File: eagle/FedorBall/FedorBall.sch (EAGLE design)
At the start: 4 parts, among them IC1 MEGA16-P

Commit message: eagle scheme scratch
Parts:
- removed SV1, SV2: (no value), con-lstb:MA05-2
- added C4: (no value), rcl:C-EU050-024X044
- added C5: 100n, rcl:C-EU050-024X044
- added C6: 0.33u, rcl:C-EU050-024X044
- added C7: 0.1u, rcl:C-EU050-024X044
- added C8: 47u, rcl:C-EU050-024X044
- added IC2: 7805T, linear:7805T
- added JP1, JP2: M05X2SHD, SparkFun:M05X2SHD
- added R1, R2, R3, R4: 10k, rcl:R-EU_0207/10
- added X1, X2: 22-23-2041, con-molex:22-23-2041
- S1: device SparkFun:TAC_SWITCHPTH -> SparkFun:TAC_SWITCHKSA_SEALED
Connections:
- new net +5V: C7.1, C8.1, IC1.AVCC, IC1.VCC, IC2.VO, JP1.2, R1.2
- new net GND: C4.2, C5.2, C6.2, C7.2, C8.2, IC1.GND, IC1.GND@1, IC2.GND, JP1.10, JP1.8, S1.1
- new net N$10: IC1.(ADC6)PA6
- new net N$11: IC1.(ADC5)PA5
- new net N$12: IC1.(ADC4)PA4
- new net N$13: IC1.(ADC3)PA3
- new net N$14: IC1.(ADC2)PA2
- new net N$15: IC1.(ADC1)PA1
- new net N$16: IC1.(ADC0)PA0
- new net N$2: C5.1, IC1.AREF
- new net N$5: IC1.(MOSI)PB5, JP1.1, R4.2
- new net N$6: C4.1, IC1.RESET, JP1.5, R1.1, S1.3
- new net N$7: IC1.(SCK)PB7, JP1.7, R2.2
- new net N$8: IC1.(MISO)PB6, JP1.9, R3.2
- new net N$9: IC1.(ADC7)PA7
- new net VCC: C6.1, IC2.VI
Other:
- moved on the sheet: IC1, S1

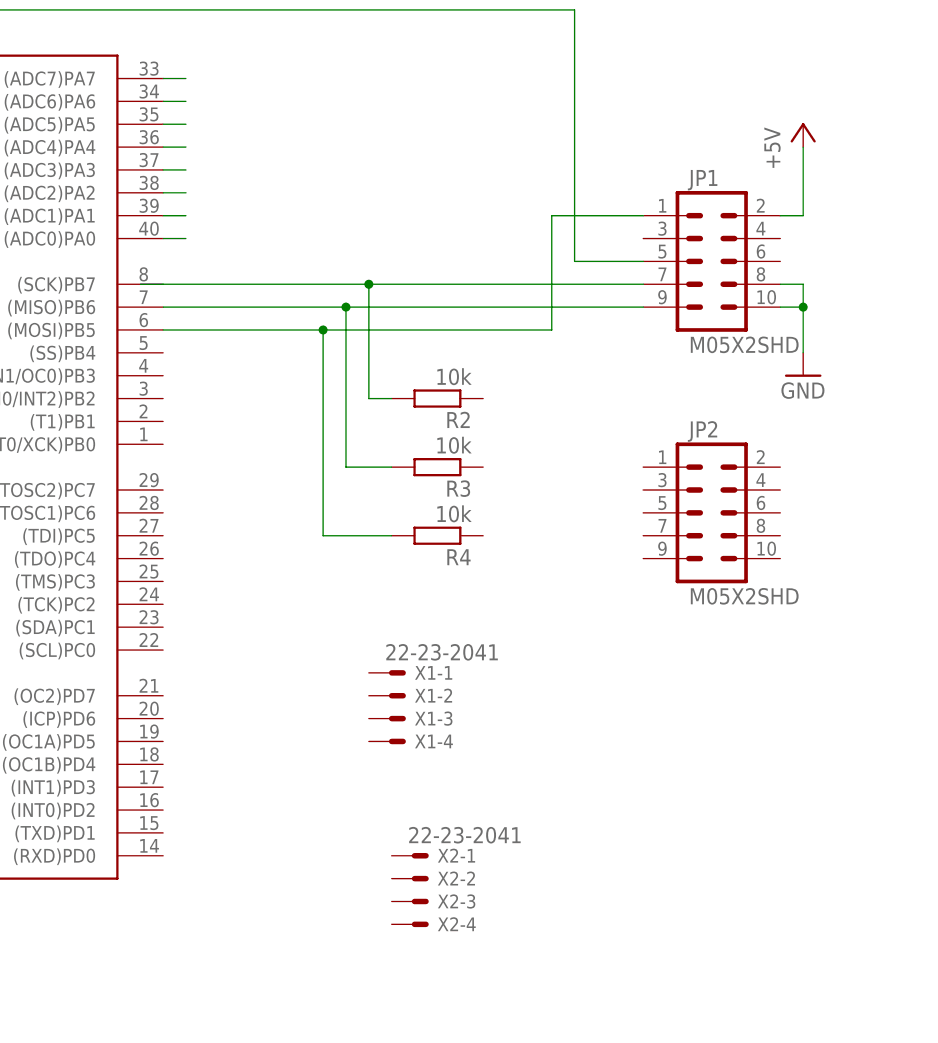
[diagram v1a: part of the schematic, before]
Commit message: update main scheme and board
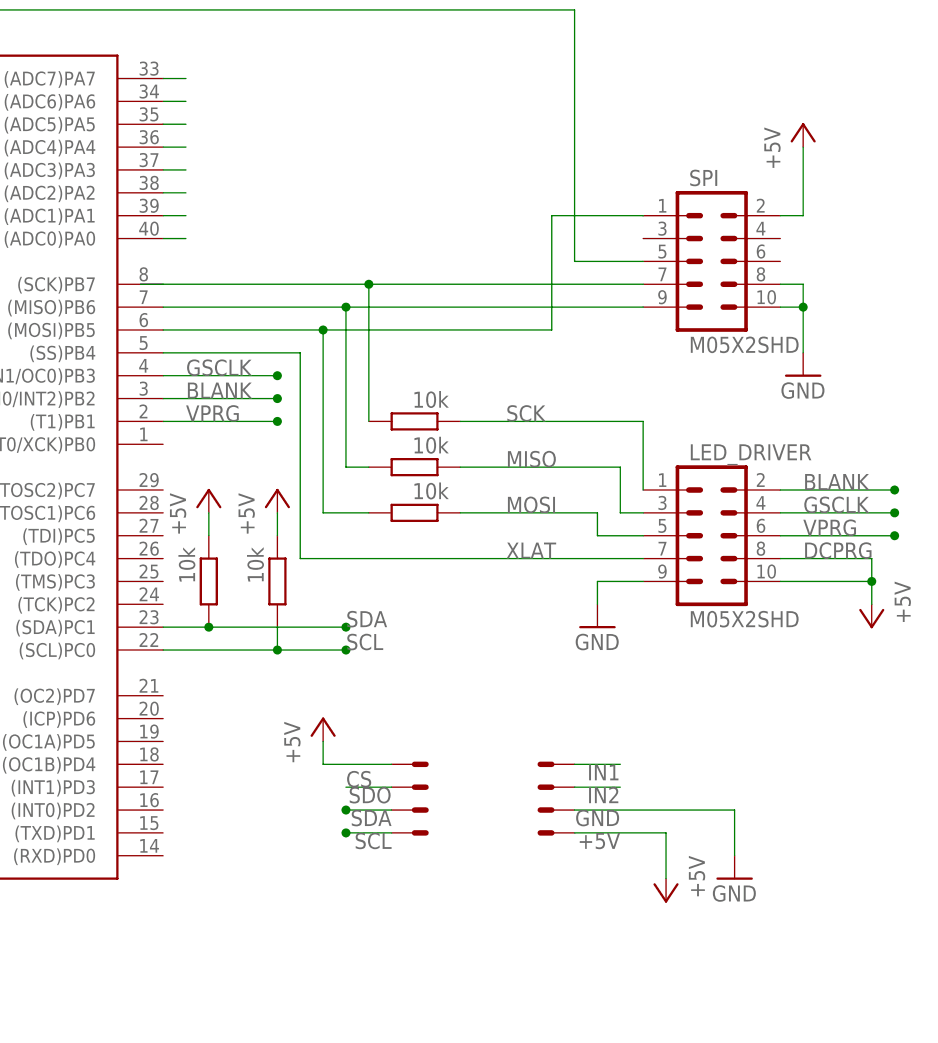
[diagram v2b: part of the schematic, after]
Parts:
- removed JP2: M05X2SHD, SparkFun:M05X2SHD
- added LED_DRIVER: M05X2SHD, SparkFun:M05X2SHD
- added R5, R6: 10k, rcl:R-EU_0207/10
- renumbered JP1 to SPI
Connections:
- new net BLANK: IC1.(AIN0/INT2)PB2, LED_DRIVER.2
- new net GSCLK: IC1.(AIN1/OC0)PB3, LED_DRIVER.4
- new net IN1: X1-4.S
- new net IN2: X1-3.S
- new net MISO: LED_DRIVER.3, R3.1
- new net MOSI: LED_DRIVER.5, R4.1
- new net SCK: LED_DRIVER.1, R2.1
- new net SCL: IC1.(SCL)PC0, R6.2, X2-1.S
- new net SDA: IC1.(SDA)PC1, R5.2, X2-2.S
- new net SDO: X2-3.S
- new net VPRG: IC1.(T1)PB1, LED_DRIVER.6
- new net XLAT: IC1.(SS)PB4, LED_DRIVER.7
- net +5V: now also LED_DRIVER.10, LED_DRIVER.8, R5.1, R6.1, X1-1.S, X2-4.S
- net GND: now also LED_DRIVER.9, X1-2.S
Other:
- note added: "CS"
- note added: "DCPRG"

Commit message: schematic tweaks
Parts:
- C4: value (none) -> 10u
- C5: value 100n -> 0.1u
- R1: value 10k -> 100k
- renumbered SPI to ISP
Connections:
- removed net IN1: X1-4.S
- removed net IN2: X1-3.S
- new net INT0: IC1.(INT1)PD3, X1-4.S
- new net INT1: IC1.(INT0)PD2, X1-3.S
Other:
- note added: "MISO"
- note added: "MOSI"
- note added: "RESET"
- note added: "SCK"
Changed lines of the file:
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@@
 <parts>
 <part name="IC1" library="atmel" deviceset="MEGA16-P" device=""/>
-<part name="C4" library="rcl" deviceset="C-EU" device="050-024X044"/>
-<part name="C5" library="rcl" deviceset="C-EU" device="050-024X044" value="100n"/>
-<part name="R1" library="rcl" deviceset="R-EU_" device="0207/10" value="10k"/>
+<part name="C4" library="rcl" deviceset="C-EU" device="050-024X044" value="10u"/>
+<part name="C5" library="rcl" deviceset="C-EU" device="050-024X044" value="0.1u"/>
+<part name="R1" library="rcl" deviceset="R-EU_" device="0207/10" value="100k"/>
 <part name="GND1" library="supply1" deviceset="GND" device=""/>
 <part name="GND3" library="supply1" deviceset="GND" device=""/>
@@
 <part name="R3" library="rcl" deviceset="R-EU_" device="0207/10" value="10k"/>
 <part name="R4" library="rcl" deviceset="R-EU_" device="0207/10" value="10k"/>
-<part name="SPI" library="SparkFun" deviceset="M05X2" device="SHD"/>
+<part name="ISP" library="SparkFun" deviceset="M05X2" device="SHD"/>
 <part name="LED_DRIVER" library="SparkFun" deviceset="M05X2" device="SHD"/>
 <part name="P+3" library="supply1" deviceset="+5V" device=""/>
@@
 <text x="86.36" y="-15.24" size="1.778" layer="95">DCPRG</text>
 <text x="35.56" y="-40.64" size="1.778" layer="95">CS</text>
+<text x="63.5" y="15.24" size="1.778" layer="95">SCK</text>
+<text x="63.5" y="12.7" size="1.778" layer="95">MISO</text>
+<text x="63.5" y="22.86" size="1.778" layer="95">MOSI</text>
+<text x="60.96" y="17.78" size="1.778" layer="95">RESET</text>
 </plain>
 <instances>
@@
 <instance part="X2" gate="-4" x="43.18" y="-38.1" smashed="yes" rot="MR180"/>
 <instance part="GND4" gate="1" x="-35.56" y="-12.7"/>
-<instance part="SUPPLY1" gate="G$1" x="-76.2" y="-38.1"/>
+<instance part="SUPPLY1" gate="G$1" x="-76.2" y="-30.48"/>
 <instance part="GND6" gate="1" x="-58.42" y="-63.5"/>
 <instance part="C6" gate="G$1" x="-71.12" y="-48.26"/>
@@
 <attribute name="VALUE" x="46.99" y="-6.858" size="1.778" layer="96" rot="R180"/>
 </instance>
-<instance part="SPI" gate="G$1" x="76.2" y="17.78"/>
+<instance part="ISP" gate="G$1" x="76.2" y="17.78"/>
 <instance part="LED_DRIVER" gate="G$1" x="76.2" y="-12.7"/>
 <instance part="P+3" gate="1" x="-35.56" y="-33.02"/>
@@
 <wire x1="83.82" y1="22.86" x2="86.36" y2="22.86" width="0.1524" layer="91"/>
 <wire x1="86.36" y1="22.86" x2="86.36" y2="30.48" width="0.1524" layer="91"/>
-<pinref part="SPI" gate="G$1" pin="2"/>
+<pinref part="ISP" gate="G$1" pin="2"/>
 </segment>
 <segment>
@@
 <wire x1="83.82" y1="12.7" x2="86.36" y2="12.7" width="0.1524" layer="91"/>
 <junction x="86.36" y="12.7"/>
-<pinref part="SPI" gate="G$1" pin="10"/>
-<pinref part="SPI" gate="G$1" pin="8"/>
+<pinref part="ISP" gate="G$1" pin="10"/>
+<pinref part="ISP" gate="G$1" pin="8"/>
 </segment>
 <segment>
@@
 <wire x1="33.02" y1="-10.16" x2="33.02" y2="10.16" width="0.1524" layer="91"/>
 <junction x="33.02" y="10.16"/>
-<pinref part="SPI" gate="G$1" pin="1"/>
+<pinref part="ISP" gate="G$1" pin="1"/>
 <wire x1="38.1" y1="-10.16" x2="33.02" y2="-10.16" width="0.1524" layer="91"/>
 </segment>
@@
 <wire x1="38.1" y1="0" x2="38.1" y2="15.24" width="0.1524" layer="91"/>
 <junction x="38.1" y="15.24"/>
-<pinref part="SPI" gate="G$1" pin="7"/>
+<pinref part="ISP" gate="G$1" pin="7"/>
 </segment>
 </net>
@@
 <wire x1="35.56" y1="-5.08" x2="35.56" y2="12.7" width="0.1524" layer="91"/>
 <junction x="35.56" y="12.7"/>
-<pinref part="SPI" gate="G$1" pin="9"/>
+<pinref part="ISP" gate="G$1" pin="9"/>
 </segment>
 </net>
@@
 <pinref part="S1" gate="S" pin="3"/>
 <wire x1="-38.1" y1="38.1" x2="-48.26" y2="38.1" width="0.1524" layer="91"/>
-<pinref part="SPI" gate="G$1" pin="5"/>
+<pinref part="ISP" gate="G$1" pin="5"/>
 </segment>
 </net>
@@
 <pinref part="IC1" gate="G$1" pin="(ADC0)PA0"/>
 <wire x1="15.24" y1="20.32" x2="17.78" y2="20.32" width="0.1524" layer="91"/>
-</segment>
-</net>
-<net name="VCC" class="0">
-<segment>
-<pinref part="SUPPLY1" gate="G$1" pin="VCC"/>
-<pinref part="IC2" gate="A1" pin="VI"/>
-<wire x1="-76.2" y1="-40.64" x2="-71.12" y2="-40.64" width="0.1524" layer="91"/>
-<pinref part="C6" gate="G$1" pin="1"/>
-<wire x1="-71.12" y1="-40.64" x2="-68.58" y2="-40.64" width="0.1524" layer="91"/>
-<wire x1="-71.12" y1="-40.64" x2="-71.12" y2="-45.72" width="0.1524" layer="91"/>
-<junction x="-71.12" y="-40.64"/>
-</segment>
-</net>
-<net name="IN2" class="0">
-<segment>
-<pinref part="X1" gate="-3" pin="S"/>
-<wire x1="60.96" y1="-40.64" x2="66.04" y2="-40.64" width="0.1524" layer="91"/>
-<label x="66.04" y="-40.64" size="1.778" layer="95" rot="R180"/>
-</segment>
-</net>
-<net name="IN1" class="0">
-<segment>
-<pinref part="X1" gate="-4" pin="S"/>
-<wire x1="60.96" y1="-38.1" x2="66.04" y2="-38.1" width="0.1524" layer="91"/>
-<label x="66.04" y="-38.1" size="1.778" layer="95" rot="R180"/>
 </segment>
 </net>
@@
 </segment>
 </net>
+<net name="VCC" class="0">
+<segment>
+<pinref part="SUPPLY1" gate="G$1" pin="VCC"/>
+<wire x1="-76.2" y1="-33.02" x2="-76.2" y2="-40.64" width="0.1524" layer="91"/>
+<pinref part="IC2" gate="A1" pin="VI"/>
+<pinref part="C6" gate="G$1" pin="1"/>
+<wire x1="-71.12" y1="-40.64" x2="-68.58" y2="-40.64" width="0.1524" layer="91"/>
+<wire x1="-71.12" y1="-40.64" x2="-71.12" y2="-45.72" width="0.1524" layer="91"/>
+<wire x1="-76.2" y1="-40.64" x2="-71.12" y2="-40.64" width="0.1524" layer="91"/>
+<junction x="-71.12" y="-40.64"/>
+</segment>
+</net>
+<net name="INT1" class="0">
+<segment>
+<pinref part="IC1" gate="G$1" pin="(INT0)PD2"/>
+<wire x1="15.24" y1="-43.18" x2="25.4" y2="-43.18" width="0.1524" layer="91"/>
+<junction x="25.4" y="-43.18"/>
+<label x="17.78" y="-43.18" size="1.778" layer="95"/>
+</segment>
+<segment>
+<pinref part="X1" gate="-3" pin="S"/>
+<wire x1="60.96" y1="-40.64" x2="66.04" y2="-40.64" width="0.1524" layer="91"/>
+<label x="66.04" y="-40.64" size="1.778" layer="95" rot="R180"/>
+<junction x="66.04" y="-40.64"/>
+</segment>
+</net>
+<net name="INT0" class="0">
+<segment>
+<pinref part="IC1" gate="G$1" pin="(INT1)PD3"/>
+<wire x1="15.24" y1="-40.64" x2="25.4" y2="-40.64" width="0.1524" layer="91"/>
+<junction x="25.4" y="-40.64"/>
+<label x="17.78" y="-40.64" size="1.778" layer="95"/>
+</segment>
+<segment>
+<pinref part="X1" gate="-4" pin="S"/>
+<wire x1="60.96" y1="-38.1" x2="66.04" y2="-38.1" width="0.1524" layer="91"/>
+<label x="66.04" y="-38.1" size="1.778" layer="95" rot="R180"/>
+<junction x="66.04" y="-38.1"/>
+</segment>
+</net>

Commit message: update scheme
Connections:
- removed net MISO: LED_DRIVER.3, R3.1
- removed net MOSI: LED_DRIVER.5, R4.1
- removed net SCK: LED_DRIVER.1, R2.1
- new net MISO_10K: LED_DRIVER.8, R3.1
- new net MOSI_10K: LED_DRIVER.9, R4.1
- new net SCK_10K: LED_DRIVER.10, R2.1
- net +5V: now also LED_DRIVER.2, LED_DRIVER.4; no longer LED_DRIVER.10, LED_DRIVER.8
- net BLANK: now also LED_DRIVER.6; no longer LED_DRIVER.2
- net GND: now also ISP.6, LED_DRIVER.1; no longer LED_DRIVER.9
- net GSCLK: now also LED_DRIVER.7; no longer LED_DRIVER.4
- net VPRG: now also LED_DRIVER.5; no longer LED_DRIVER.6
- net XLAT: now also LED_DRIVER.3; no longer LED_DRIVER.7
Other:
- moved on the sheet: LED_DRIVER
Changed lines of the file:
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@@
 <part name="GND2" library="supply1" deviceset="GND" device=""/>
 <part name="P+8" library="supply1" deviceset="+5V" device=""/>
+<part name="P+9" library="supply1" deviceset="+5V" device=""/>
 <part name="GND7" library="supply1" deviceset="GND" device=""/>
-<part name="P+10" library="supply1" deviceset="+5V" device=""/>
 </parts>
 <sheets>
 <sheet>
 <plain>
-<text x="86.36" y="-15.24" size="1.778" layer="95">DCPRG</text>
+<text x="83.82" y="-17.78" size="1.778" layer="95">DCPRG</text>
 <text x="35.56" y="-40.64" size="1.778" layer="95">CS</text>
 <text x="63.5" y="15.24" size="1.778" layer="95">SCK</text>
@@
 </instance>
 <instance part="ISP" gate="G$1" x="76.2" y="17.78"/>
-<instance part="LED_DRIVER" gate="G$1" x="76.2" y="-12.7"/>
+<instance part="LED_DRIVER" gate="G$1" x="76.2" y="-20.32"/>
 <instance part="P+3" gate="1" x="-35.56" y="-33.02"/>
 <instance part="R5" gate="G$1" x="20.32" y="-17.78" smashed="yes" rot="R270">
@@
 <instance part="GND2" gate="1" x="78.74" y="-50.8"/>
 <instance part="P+8" gate="1" x="33.02" y="-33.02"/>
-<instance part="GND7" gate="1" x="63.5" y="-22.86"/>
-<instance part="P+10" gate="1" x="93.98" y="-22.86" rot="R180"/>
+<instance part="P+9" gate="1" x="93.98" y="-5.08"/>
+<instance part="GND7" gate="1" x="66.04" y="-7.62" rot="R180"/>
 </instances>
 <busses>
@@
 </segment>
 <segment>
-<pinref part="LED_DRIVER" gate="G$1" pin="10"/>
+<pinref part="LED_DRIVER" gate="G$1" pin="2"/>
+<wire x1="83.82" y1="-15.24" x2="93.98" y2="-15.24" width="0.1524" layer="91"/>
+<wire x1="93.98" y1="-15.24" x2="93.98" y2="-7.62" width="0.1524" layer="91"/>
+<pinref part="LED_DRIVER" gate="G$1" pin="4"/>
 <wire x1="83.82" y1="-17.78" x2="93.98" y2="-17.78" width="0.1524" layer="91"/>
-<pinref part="P+10" gate="1" pin="+5V"/>
-<wire x1="93.98" y1="-17.78" x2="93.98" y2="-20.32" width="0.1524" layer="91"/>
-<pinref part="LED_DRIVER" gate="G$1" pin="8"/>
-<wire x1="83.82" y1="-15.24" x2="93.98" y2="-15.24" width="0.1524" layer="91"/>
-<wire x1="93.98" y1="-15.24" x2="93.98" y2="-17.78" width="0.1524" layer="91"/>
-<junction x="93.98" y="-17.78"/>
+<wire x1="93.98" y1="-17.78" x2="93.98" y2="-15.24" width="0.1524" layer="91"/>
+<junction x="93.98" y="-15.24"/>
+<pinref part="P+9" gate="1" pin="+5V"/>
 </segment>
 </net>
@@
 <pinref part="ISP" gate="G$1" pin="10"/>
 <pinref part="ISP" gate="G$1" pin="8"/>
+<pinref part="ISP" gate="G$1" pin="6"/>
+<wire x1="83.82" y1="17.78" x2="86.36" y2="17.78" width="0.1524" layer="91"/>
+<wire x1="86.36" y1="17.78" x2="86.36" y2="15.24" width="0.1524" layer="91"/>
+<junction x="86.36" y="15.24"/>
 </segment>
 <segment>
@@
 </segment>
 <segment>
-<pinref part="LED_DRIVER" gate="G$1" pin="9"/>
+<pinref part="LED_DRIVER" gate="G$1" pin="1"/>
+<wire x1="68.58" y1="-15.24" x2="66.04" y2="-15.24" width="0.1524" layer="91"/>
+<wire x1="66.04" y1="-15.24" x2="66.04" y2="-10.16" width="0.1524" layer="91"/>
 <pinref part="GND7" gate="1" pin="GND"/>
-<wire x1="68.58" y1="-17.78" x2="63.5" y2="-17.78" width="0.1524" layer="91"/>
-<wire x1="63.5" y1="-17.78" x2="63.5" y2="-20.32" width="0.1524" layer="91"/>
 </segment>
 </net>
@@
 </segment>
 </net>
-<net name="SCK" class="0">
-<segment>
-<pinref part="R2" gate="G$1" pin="1"/>
-<wire x1="48.26" y1="0" x2="68.58" y2="0" width="0.1524" layer="91"/>
-<wire x1="68.58" y1="0" x2="68.58" y2="-7.62" width="0.1524" layer="91"/>
-<pinref part="LED_DRIVER" gate="G$1" pin="1"/>
-<label x="53.34" y="0" size="1.778" layer="95"/>
-</segment>
-</net>
-<net name="MISO" class="0">
-<segment>
-<pinref part="R3" gate="G$1" pin="1"/>
-<wire x1="48.26" y1="-5.08" x2="66.04" y2="-5.08" width="0.1524" layer="91"/>
-<wire x1="66.04" y1="-5.08" x2="66.04" y2="-10.16" width="0.1524" layer="91"/>
-<pinref part="LED_DRIVER" gate="G$1" pin="3"/>
-<wire x1="66.04" y1="-10.16" x2="68.58" y2="-10.16" width="0.1524" layer="91"/>
-<label x="53.34" y="-5.08" size="1.778" layer="95"/>
-</segment>
-</net>
-<net name="MOSI" class="0">
-<segment>
-<pinref part="R4" gate="G$1" pin="1"/>
-<wire x1="48.26" y1="-10.16" x2="63.5" y2="-10.16" width="0.1524" layer="91"/>
-<wire x1="63.5" y1="-10.16" x2="63.5" y2="-12.7" width="0.1524" layer="91"/>
-<pinref part="LED_DRIVER" gate="G$1" pin="5"/>
-<wire x1="63.5" y1="-12.7" x2="68.58" y2="-12.7" width="0.1524" layer="91"/>
-<label x="53.34" y="-10.16" size="1.778" layer="95"/>
-</segment>
-</net>
 <net name="BLANK" class="0">
-<segment>
-<pinref part="LED_DRIVER" gate="G$1" pin="2"/>
-<wire x1="83.82" y1="-7.62" x2="96.52" y2="-7.62" width="0.1524" layer="91"/>
-<label x="86.36" y="-7.62" size="1.778" layer="95"/>
-<junction x="96.52" y="-7.62"/>
-</segment>
 <segment>
 <pinref part="IC1" gate="G$1" pin="(AIN0/INT2)PB2"/>
@@
 <label x="17.78" y="2.54" size="1.778" layer="95"/>
 </segment>
+<segment>
+<pinref part="LED_DRIVER" gate="G$1" pin="6"/>
+<wire x1="83.82" y1="-20.32" x2="93.98" y2="-20.32" width="0.1524" layer="91"/>
+<junction x="93.98" y="-20.32"/>
+<label x="83.82" y="-20.32" size="1.778" layer="95"/>
+</segment>
 </net>
 <net name="GSCLK" class="0">
-<segment>
-<pinref part="LED_DRIVER" gate="G$1" pin="4"/>
-<wire x1="83.82" y1="-10.16" x2="96.52" y2="-10.16" width="0.1524" layer="91"/>
-<label x="86.36" y="-10.16" size="1.778" layer="95"/>
-<junction x="96.52" y="-10.16"/>
-</segment>
 <segment>
 <pinref part="IC1" gate="G$1" pin="(AIN1/OC0)PB3"/>
@@
 <label x="17.78" y="5.08" size="1.778" layer="95"/>
 </segment>
+<segment>
+<pinref part="LED_DRIVER" gate="G$1" pin="7"/>
+<wire x1="68.58" y1="-22.86" x2="60.96" y2="-22.86" width="0.1524" layer="91"/>
+<junction x="60.96" y="-22.86"/>
+<label x="63.5" y="-22.86" size="1.778" layer="95"/>
+</segment>
 </net>
 <net name="VPRG" class="0">
-<segment>
-<pinref part="LED_DRIVER" gate="G$1" pin="6"/>
-<wire x1="83.82" y1="-12.7" x2="96.52" y2="-12.7" width="0.1524" layer="91"/>
-<label x="86.36" y="-12.7" size="1.778" layer="95"/>
-<junction x="96.52" y="-12.7"/>
-</segment>
 <segment>
 <pinref part="IC1" gate="G$1" pin="(T1)PB1"/>
@@
 <label x="17.78" y="0" size="1.778" layer="95"/>
 </segment>
-</net>
-<net name="XLAT" class="0">
-<segment>
-<pinref part="LED_DRIVER" gate="G$1" pin="7"/>
-<wire x1="68.58" y1="-15.24" x2="30.48" y2="-15.24" width="0.1524" layer="91"/>
-<label x="53.34" y="-15.24" size="1.778" layer="95"/>
-<pinref part="IC1" gate="G$1" pin="(SS)PB4"/>
-<wire x1="15.24" y1="7.62" x2="30.48" y2="7.62" width="0.1524" layer="91"/>
-<wire x1="30.48" y1="7.62" x2="30.48" y2="-15.24" width="0.1524" layer="91"/>
+<segment>
+<pinref part="LED_DRIVER" gate="G$1" pin="5"/>
+<wire x1="68.58" y1="-20.32" x2="60.96" y2="-20.32" width="0.1524" layer="91"/>
+<junction x="60.96" y="-20.32"/>
+<label x="63.5" y="-20.32" size="1.778" layer="95"/>
 </segment>
 </net>
@@
 </segment>
 </net>
+<net name="XLAT" class="0">
+<segment>
+<pinref part="IC1" gate="G$1" pin="(SS)PB4"/>
+<wire x1="15.24" y1="7.62" x2="27.94" y2="7.62" width="0.1524" layer="91"/>
+<junction x="27.94" y="7.62"/>
+<label x="17.78" y="7.62" size="1.778" layer="95"/>
+</segment>
+<segment>
+<pinref part="LED_DRIVER" gate="G$1" pin="3"/>
+<wire x1="68.58" y1="-17.78" x2="60.96" y2="-17.78" width="0.1524" layer="91"/>
+<junction x="60.96" y="-17.78"/>
+<label x="63.5" y="-17.78" size="1.778" layer="95"/>
+</segment>
+</net>
+<net name="SCK_10K" class="0">
+<segment>
+<pinref part="R2" gate="G$1" pin="1"/>
+<wire x1="48.26" y1="0" x2="55.88" y2="0" width="0.1524" layer="91"/>
+<junction x="55.88" y="0"/>
+<label x="48.26" y="0" size="1.778" layer="95"/>
+</segment>
+<segment>
+<pinref part="LED_DRIVER" gate="G$1" pin="10"/>
+<wire x1="83.82" y1="-25.4" x2="93.98" y2="-25.4" width="0.1524" layer="91"/>
+<junction x="93.98" y="-25.4"/>
+<label x="83.82" y="-25.4" size="1.778" layer="95"/>
+</segment>
+</net>
+<net name="MISO_10K" class="0">
+<segment>
+<pinref part="R3" gate="G$1" pin="1"/>
+<wire x1="48.26" y1="-5.08" x2="55.88" y2="-5.08" width="0.1524" layer="91"/>
+<junction x="55.88" y="-5.08"/>
+<label x="48.26" y="-5.08" size="1.778" layer="95"/>
+</segment>
+<segment>
+<pinref part="LED_DRIVER" gate="G$1" pin="8"/>
+<wire x1="83.82" y1="-22.86" x2="93.98" y2="-22.86" width="0.1524" layer="91"/>
+<junction x="93.98" y="-22.86"/>
+<label x="83.82" y="-22.86" size="1.778" layer="95"/>
+</segment>
+</net>
+<net name="MOSI_10K" class="0">
+<segment>
+<pinref part="R4" gate="G$1" pin="1"/>
+<wire x1="48.26" y1="-10.16" x2="55.88" y2="-10.16" width="0.1524" layer="91"/>
+<junction x="55.88" y="-10.16"/>
+<label x="48.26" y="-10.16" size="1.778" layer="95"/>
+</segment>
+<segment>
+<pinref part="LED_DRIVER" gate="G$1" pin="9"/>
+<wire x1="68.58" y1="-25.4" x2="60.96" y2="-25.4" width="0.1524" layer="91"/>
+<junction x="60.96" y="-25.4"/>
+<label x="63.5" y="-25.4" size="1.778" layer="95"/>
+</segment>
+</net>
